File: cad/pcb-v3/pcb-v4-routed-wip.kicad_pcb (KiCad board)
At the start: 4 copper layers, 19.3 x 19.3 mm, 50 parts

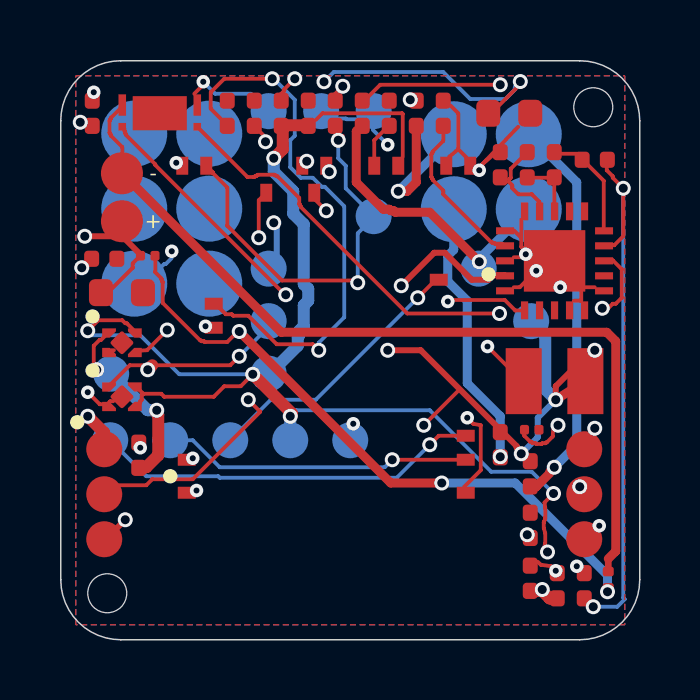
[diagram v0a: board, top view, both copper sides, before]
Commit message: Via stitching: 50 GND vias, no tracks -- the safe way to connect the pours
The F.Cu pour is fragmented into 13 islands and B.Cu into 5. An island with no
via to the In2.Cu plane is orphaned copper, and island_removal_mode 0 deletes
it -- so a GND pad touching such an island gains nothing from the pour.

Stitched 50 GND vias on a 0.25 mm grid wherever legal. This is the standard
technique and, unlike the taps I hand-placed and had to revert, it carries no
routing risk at all: a via with no track cannot cross another net. The only
question is whether each hole is legal, and that is a point test.

Every via checked against: board edge (0.30), the R2.0 corner arcs, the antenna
keep-out's 'vias not_allowed' polygons, J4/J11 pogo contacts INCLUDING J4.5
which is itself GND, every non-GND pad WITH ROTATION APPLIED, every track, and
hole-to-hole against existing vias. All the traps this board has produced today,
in one predicate.

  sexp_check  PARSE OK, 130 vias
  check_board 0 different-net pairs closer than 0.1
  check 22    130 vias vs 10 pogo pads, all clear

Open-pad count will not move until the pours re-fill around the new vias.
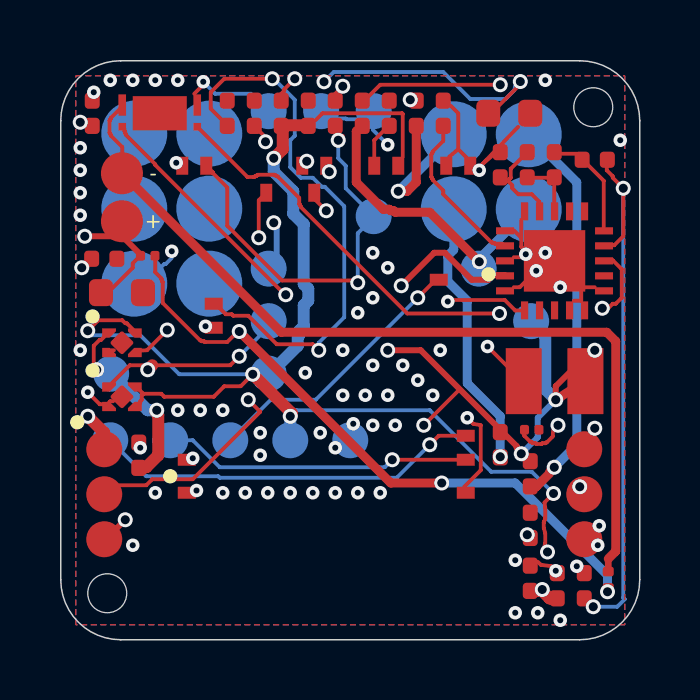
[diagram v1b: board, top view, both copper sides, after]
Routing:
- net GND: vias 18 -> 68
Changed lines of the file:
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@@
 	)
 	(embedded_fonts no)
+	(via (at -8.0000 -9.0000) (size 0.45) (drill 0.2) (layers "F.Cu" "B.Cu") (net "GND"))
+	(via (at -7.2500 -9.0000) (size 0.45) (drill 0.2) (layers "F.Cu" "B.Cu") (net "GND"))
+	(via (at -6.5000 -9.0000) (size 0.45) (drill 0.2) (layers "F.Cu" "B.Cu") (net "GND"))
+	(via (at -5.7500 -9.0000) (size 0.45) (drill 0.2) (layers "F.Cu" "B.Cu") (net "GND"))
+	(via (at 6.5000 -9.0000) (size 0.45) (drill 0.2) (layers "F.Cu" "B.Cu") (net "GND"))
+	(via (at 9.0000 -7.0000) (size 0.45) (drill 0.2) (layers "F.Cu" "B.Cu") (net "GND"))
+	(via (at -9.0000 -6.7500) (size 0.45) (drill 0.2) (layers "F.Cu" "B.Cu") (net "GND"))
+	(via (at -9.0000 -6.0000) (size 0.45) (drill 0.2) (layers "F.Cu" "B.Cu") (net "GND"))
+	(via (at -9.0000 -5.2500) (size 0.45) (drill 0.2) (layers "F.Cu" "B.Cu") (net "GND"))
+	(via (at -9.0000 -4.5000) (size 0.45) (drill 0.2) (layers "F.Cu" "B.Cu") (net "GND"))
+	(via (at 0.7500 -3.2500) (size 0.45) (drill 0.2) (layers "F.Cu" "B.Cu") (net "GND"))
+	(via (at 6.5000 -3.2500) (size 0.45) (drill 0.2) (layers "F.Cu" "B.Cu") (net "GND"))
+	(via (at 1.2500 -2.7500) (size 0.45) (drill 0.2) (layers "F.Cu" "B.Cu") (net "GND"))
+	(via (at 0.7500 -1.7500) (size 0.45) (drill 0.2) (layers "F.Cu" "B.Cu") (net "GND"))
+	(via (at 0.2500 -1.2500) (size 0.45) (drill 0.2) (layers "F.Cu" "B.Cu") (net "GND"))
+	(via (at -9.0000 0.0000) (size 0.45) (drill 0.2) (layers "F.Cu" "B.Cu") (net "GND"))
+	(via (at -0.2500 0.0000) (size 0.45) (drill 0.2) (layers "F.Cu" "B.Cu") (net "GND"))
+	(via (at 3.0000 0.0000) (size 0.45) (drill 0.2) (layers "F.Cu" "B.Cu") (net "GND"))
+	(via (at 0.7500 0.5000) (size 0.45) (drill 0.2) (layers "F.Cu" "B.Cu") (net "GND"))
+	(via (at 1.7500 0.5000) (size 0.45) (drill 0.2) (layers "F.Cu" "B.Cu") (net "GND"))
+	(via (at -1.5000 0.7500) (size 0.45) (drill 0.2) (layers "F.Cu" "B.Cu") (net "GND"))
+	(via (at 2.2500 1.0000) (size 0.45) (drill 0.2) (layers "F.Cu" "B.Cu") (net "GND"))
+	(via (at -0.2500 1.5000) (size 0.45) (drill 0.2) (layers "F.Cu" "B.Cu") (net "GND"))
+	(via (at 0.5000 1.5000) (size 0.45) (drill 0.2) (layers "F.Cu" "B.Cu") (net "GND"))
+	(via (at 1.2500 1.5000) (size 0.45) (drill 0.2) (layers "F.Cu" "B.Cu") (net "GND"))
+	(via (at 2.7500 1.5000) (size 0.45) (drill 0.2) (layers "F.Cu" "B.Cu") (net "GND"))
+	(via (at -5.7500 2.0000) (size 0.45) (drill 0.2) (layers "F.Cu" "B.Cu") (net "GND"))
+	(via (at -5.0000 2.0000) (size 0.45) (drill 0.2) (layers "F.Cu" "B.Cu") (net "GND"))
+	(via (at -4.2500 2.0000) (size 0.45) (drill 0.2) (layers "F.Cu" "B.Cu") (net "GND"))
+	(via (at 0.7500 2.5000) (size 0.45) (drill 0.2) (layers "F.Cu" "B.Cu") (net "GND"))
+	(via (at 1.5000 2.5000) (size 0.45) (drill 0.2) (layers "F.Cu" "B.Cu") (net "GND"))
+	(via (at -3.0000 2.7500) (size 0.45) (drill 0.2) (layers "F.Cu" "B.Cu") (net "GND"))
+	(via (at -1.0000 2.7500) (size 0.45) (drill 0.2) (layers "F.Cu" "B.Cu") (net "GND"))
+	(via (at -0.5000 3.2500) (size 0.45) (drill 0.2) (layers "F.Cu" "B.Cu") (net "GND"))
+	(via (at -3.0000 3.5000) (size 0.45) (drill 0.2) (layers "F.Cu" "B.Cu") (net "GND"))
+	(via (at -6.5000 4.7500) (size 0.45) (drill 0.2) (layers "F.Cu" "B.Cu") (net "GND"))
+	(via (at -4.2500 4.7500) (size 0.45) (drill 0.2) (layers "F.Cu" "B.Cu") (net "GND"))
+	(via (at -3.5000 4.7500) (size 0.45) (drill 0.2) (layers "F.Cu" "B.Cu") (net "GND"))
+	(via (at -2.7500 4.7500) (size 0.45) (drill 0.2) (layers "F.Cu" "B.Cu") (net "GND"))
+	(via (at -2.0000 4.7500) (size 0.45) (drill 0.2) (layers "F.Cu" "B.Cu") (net "GND"))
+	(via (at -1.2500 4.7500) (size 0.45) (drill 0.2) (layers "F.Cu" "B.Cu") (net "GND"))
+	(via (at -0.5000 4.7500) (size 0.45) (drill 0.2) (layers "F.Cu" "B.Cu") (net "GND"))
+	(via (at 0.2500 4.7500) (size 0.45) (drill 0.2) (layers "F.Cu" "B.Cu") (net "GND"))
+	(via (at 1.0000 4.7500) (size 0.45) (drill 0.2) (layers "F.Cu" "B.Cu") (net "GND"))
+	(via (at -7.2500 6.5000) (size 0.45) (drill 0.2) (layers "F.Cu" "B.Cu") (net "GND"))
+	(via (at 8.2500 6.5000) (size 0.45) (drill 0.2) (layers "F.Cu" "B.Cu") (net "GND"))
+	(via (at 5.5000 7.0000) (size 0.45) (drill 0.2) (layers "F.Cu" "B.Cu") (net "GND"))
+	(via (at 5.5000 8.7500) (size 0.45) (drill 0.2) (layers "F.Cu" "B.Cu") (net "GND"))
+	(via (at 6.2500 8.7500) (size 0.45) (drill 0.2) (layers "F.Cu" "B.Cu") (net "GND"))
+	(via (at 7.0000 9.0000) (size 0.45) (drill 0.2) (layers "F.Cu" "B.Cu") (net "GND"))
 )

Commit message: Remove 13 stitching vias that reached into the antenna keep-out
I tested each via's CENTRE against the keep-out polygon instead of growing the
polygon by the via radius. A via centred at y = 4.75 with a 0.225 radius reaches
4.975, and the keep-out starts at 4.95. Thirteen of the fifty landed that way.

gnd_taps.py carries a comment about precisely this, which I read this morning:
'poly_mask marks cells whose CENTRE is inside; a via centred 0.25 mm OUTSIDE
the antenna keep-out still puts 0.05 mm of copper inside it. A keep-out applies
to the copper, not to the centre point.' Same mistake, same day, in a predicate
I wrote from scratch instead of reusing the one that already had the fix.

Removed by testing the buffered via against the union of the keep-out polygons.
117 vias remain. Checks 7 and 22 both PASS, check_board 0 violations.

The 37 surviving stitching vias did NOT reduce the open-pad count -- still 7.
So pour fragmentation was not what was stranding C3/C5/C9/C12/U4.2 after all;
that hypothesis is dead and the pads are isolated for some other reason.
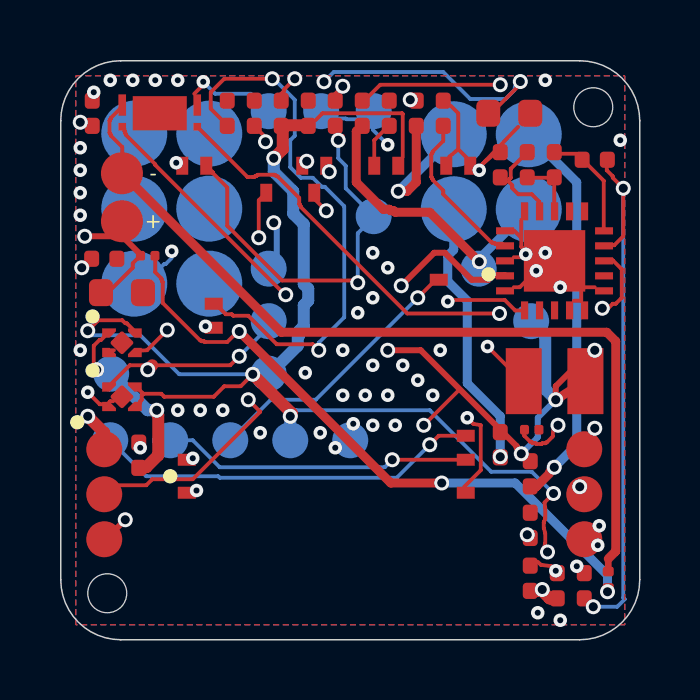
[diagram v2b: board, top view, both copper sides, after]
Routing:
- net GND: vias 68 -> 55

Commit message: U5 placement gains a second objective; PCM_VM routes, board rebuilt clean
U5's position came from ONE term -- minimise S1 -> BT1-2 -- and that drove it
into the bottom-left corner and straight into the J4 pogo block: U5.3 (V-) was
0.461 mm from J4.2, inside its no-via ring, and U5.4 (S2, GND) 1.128 mm from a
pogo pad. Fatal twice. S2 returns every milliamp on the board and needs a solid
path to the plane, which no ring permits. And R9 is 2.7k from PCM_VM to GND, so
it carries a GND pad and the ring ban correctly kept it away from the pin it
connects to -- PCM_VM routed with zero copper.

The trial loop now rejects any U5 position where S2 sits in a ring or V- has no
legal neighbourhood, as cheap point tests before the expensive packer trial.

  U5 -> (-4.65,-7.90), S1->BT1-2 = 2.85 mm (was 2.28 into the pogo block)
  stage 1 routing        9/9 SUCCESS, PCM_VM included
  nets with copper       29 of 30, only GND empty as intended
  0402 packer            23/23

Board rebuilt end to end from the fixed script and finished properly: GND pours
cloned onto F.Cu and B.Cu at 0.10 clearance (not the plane's 0.25, which was
the mistake last time), and the one dangling stub removed by looping on
preflight's own report.

  check_board   0 different-net pairs closer than 0.10
  sexp_check    PARSE OK, 17 zones, 697 segments, 101 vias
  blockers      6 (8 open pads), 17 and 18 -- and 17/18 are the fill

Trading 0.57 mm of cell path for a PCM that is out of the pogo block and whose
sense leg can reach its own pin is clearly the right side of that bargain.
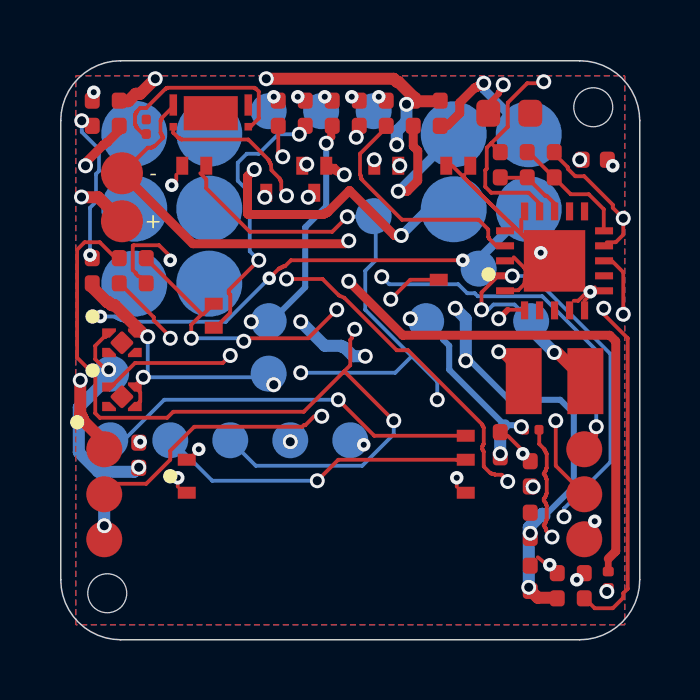
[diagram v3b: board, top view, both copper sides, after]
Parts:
- moved R3 16.8 mm to (-7.70, -7.90)
- moved R9 16.3 mm to (-6.80, -7.45), turned to 90 degrees
- moved C3 15.6 mm to (6.00, 5.84)
- moved R8 14.1 mm to (6.05, 2.65)
- moved C5 13.6 mm to (5.00, 3.15), turned to 90 degrees
- moved R2 12.4 mm to (3.00, -7.90)
- moved R6 8.91 mm to (-6.80, -2.65)
- moved R7 8.91 mm to (-7.70, -2.65)
- moved R4 8.20 mm to (-8.60, -2.65)
- moved R5 7.10 mm to (-1.50, -7.90)
- moved TP3 5.53 mm to (2.53, -0.97)
- moved C12 4.87 mm to (-8.60, -7.90), turned to 90 degrees
- moved ROV1 3.15 mm to (8.15, -6.35), turned to 0 degrees
- moved C6 2.60 mm to (-0.60, -7.90)
- moved C4 1.90 mm to (1.20, -7.90)
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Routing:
- net BL_FLAG: track 51.3 -> 16.6 mm, vias 3 -> 4
- net PCM_VM: track 19.0 -> 6.81 mm, vias 2 -> 0
- net BL_RETURN: track 9.51 -> 21.5 mm, vias 1 -> 4
- net RESET: track 19.6 -> 30.4 mm, vias 2 -> 3
- net VBAT: track 12.4 -> 22.4 mm, vias 2 -> 6
- net HARV_2: track 13.1 -> 4.56 mm
- net HARV_3: track 9.06 -> 17.3 mm, vias 1 -> 3
- net VBAT_OK: track 29.5 -> 37.5 mm, vias 3 -> 5
- net VBAT_OV_SET: track 2.90 -> 10.4 mm, vias 0 -> 2
- net SENSOR_SW_EN: track 7.11 -> 0.11 mm, vias 2 -> 1
- net VSTOR: track 45.7 -> 40.4 mm, vias 7 -> 9
- net GND: track 19.8 -> 15.0 mm, vias 55 -> 19
- net PCM_VDD: track 31.0 -> 27.6 mm, vias 4 -> 5
- net VBAT_SENSE: track 25.4 -> 22.3 mm
- net VREF_SAMP: track 5.26 -> 8.02 mm
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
